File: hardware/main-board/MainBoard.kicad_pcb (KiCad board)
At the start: 4 copper layers, 145 parts, among them J1 Conn_01x03_Pin, J10 USB_C_Receptacle_USB2.0_14P, J11 Conn_02x05_Odd_Even, J12 Conn_01x02_Pin, J13 Conn_01x02_Pin, J2 Conn_01x03_Pin, J3 Conn_01x03_Pin, J4 Conn_01x03_Pin, J5 Conn_01x02_Pin, J6 Conn_01x02_Pin, J7 Conn_01x02_Pin, J8 Conn_01x02_Pin, J9 Barrel_Jack, SW1 SW_SP3T, SW2 SW_SP3T, SW3 SW_SPST, SW4 SW_SPST, U1 CD22M3494MQZ, U10 TL071, U11 CD22M3494MQZ, U12 CD22M3494MQZ, U13 TL071, U14 AD5263BRUZ200, U15 AD5263BRUZ200, U16 TL071, U17 CD22M3494MQZ, U18 CD22M3494MQZ, U19 TL071, U2 TL081, U20 AD5263BRUZ200, U21 AD5263BRUZ200, U22 TL071, U23 CD22M3494MQZ, U24 CD22M3494MQZ, U25 TL071, U26 AD5263BRUZ200, U27 AD5263BRUZ200, U28 TL071, U29 CD22M3494MQZ, U3 TL071, U30 CD22M3494MQZ, U31 XTPS55285VALR, U32 TPS54202DDC, U33 LM2776, U34 74HC164, U35 FT232RL, U36 74HC164, U37 STM32F091RCTx, U38 74HC164, U4 TL071, U5 TL071, U6 TL071, U7 TL071, U8 AD5263BRUZ200, U9 AD5263BRUZ200

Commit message: Standard cell 1 finalizations
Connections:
- net /STD/Y1 renamed /STD_Y1
- U1 pad 29: /STD/Y2 -> /STD_Y0
- U1 pad 31: /STD/Y0 -> /STD_Y2
- U11 pad 32: /STD/Y0 -> /STD_Y0
- U11 pad 37: /STD/Y2 -> /STD_Y2
- U12 pad 13: /STD/Y2 -> /STD_Y2
- U12 pad 17: /STD/Y0 -> /STD_Y0
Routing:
- net /STD_Y0: track 0.00 -> 110.1 mm, vias 0 -> 2
- net /STD_Y2: track 0.00 -> 105.1 mm, vias 0 -> 2
- net /MicroController/MT_CS_6: track 14.5 -> 109.1 mm, vias 0 -> 4
- net /MicroController/BRUZ_NCS_2: track 0.00 -> 88.0 mm, vias 0 -> 4
- net /STD_Y1: track 47.8 -> 107.6 mm
- net /MicroController/MT_CS_3: track 71.4 -> 128.7 mm, vias 2 -> 4
- net /STD/Y0: track 52.1 -> 0.00 mm, vias 2 -> 0
- net /STD/Y2: track 44.1 -> 0.00 mm, vias 2 -> 0
- net /MicroController/MT_DAT: track 229.8 -> 272.4 mm, vias 16 -> 17
- net /MicroController/BRUZ_NCS_0: track 33.6 -> 64.1 mm, vias 0 -> 2
- net /MicroController/MT_CS_8: track 46.7 -> 19.5 mm
- net /MicroController/MT_CS_7: track 70.4 -> 50.7 mm
- net /Cell_0_Buff: track 4.95 -> 7.70 mm

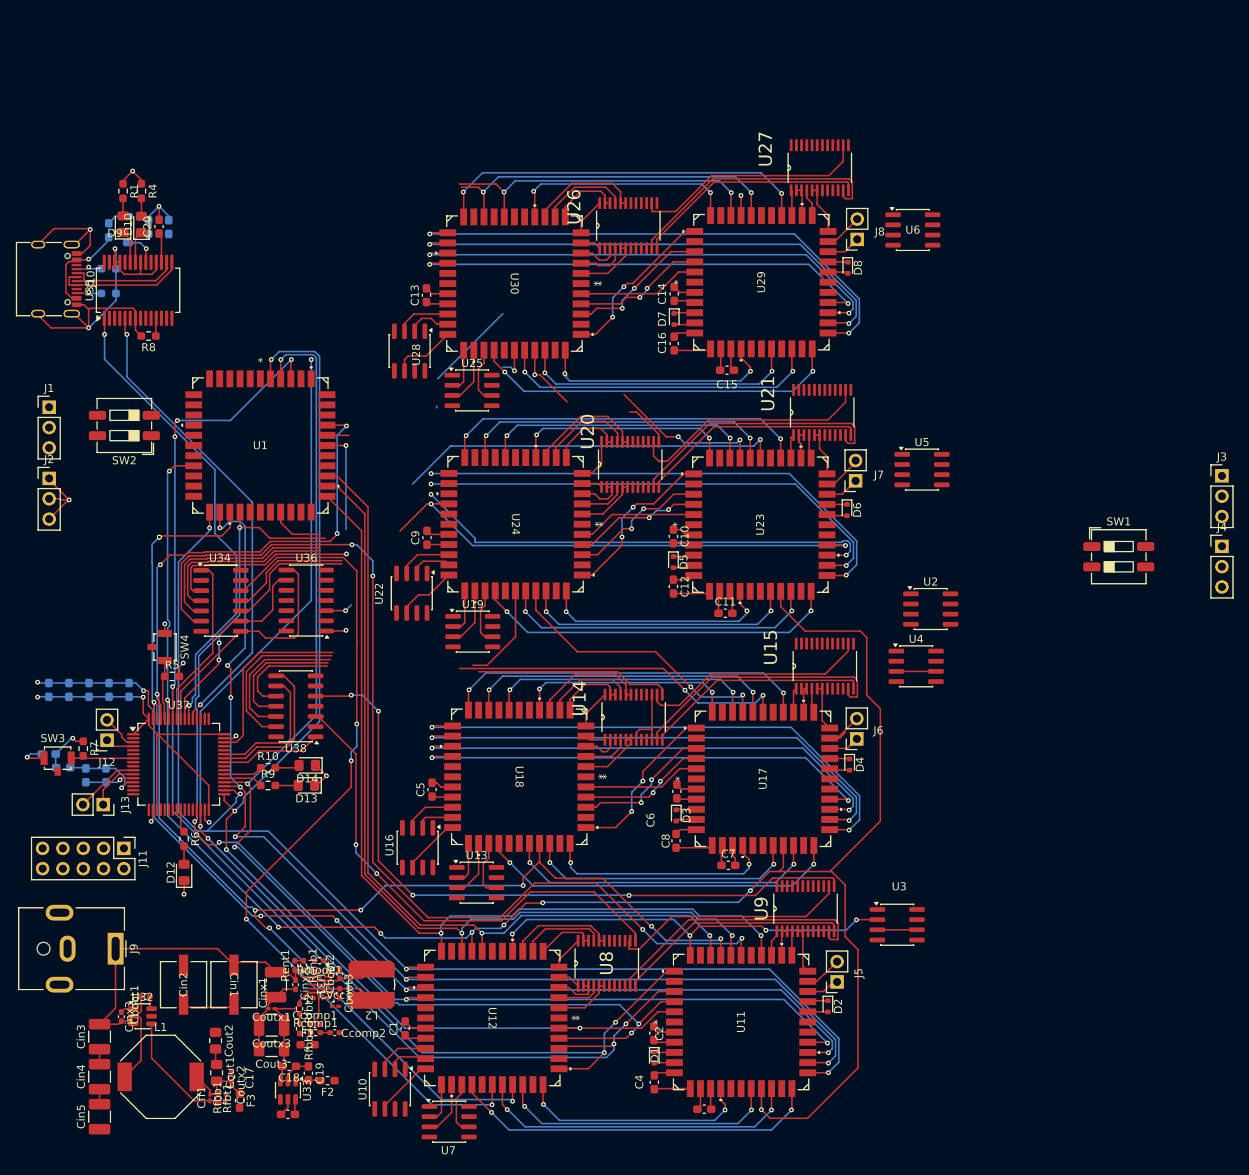
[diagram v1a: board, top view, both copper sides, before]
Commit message: linked outside AX and AY and other controls
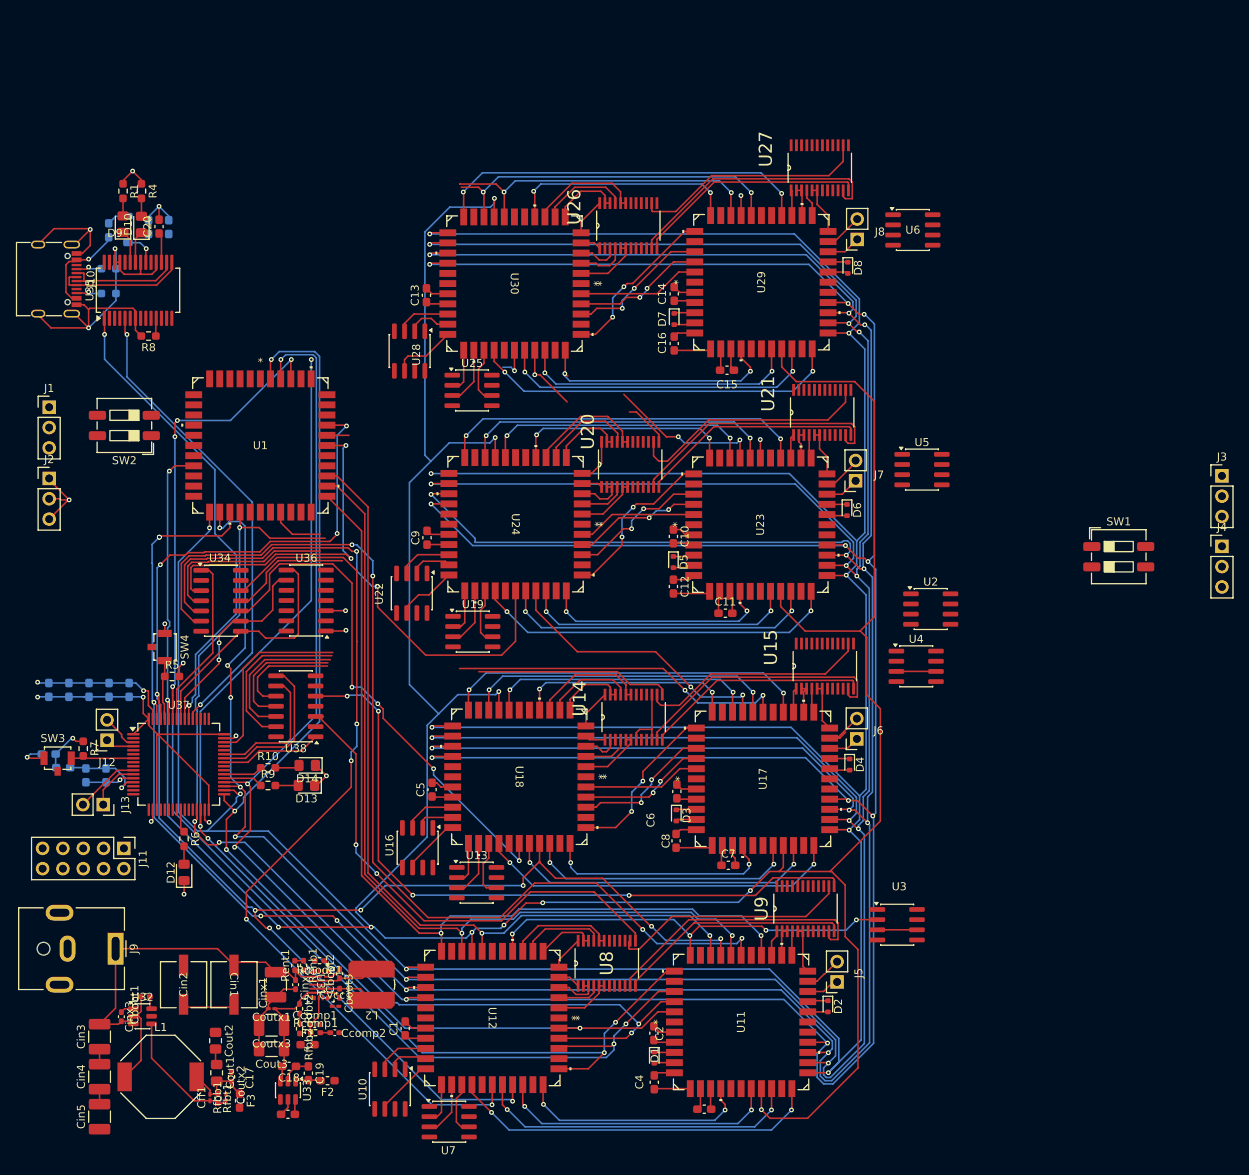
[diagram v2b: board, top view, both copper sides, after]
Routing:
- net /MicroController/MT_STB: track 238.4 -> 414.3 mm, vias 9 -> 12
- net /MicroController/MT_AY0: track 335.7 -> 449.5 mm, vias 13 -> 16
- net /MicroController/MT_AY1: track 333.0 -> 444.7 mm, vias 11 -> 14
- net /MicroController/MT_AX2: track 333.5 -> 441.1 mm, vias 13 -> 16
- net /MicroController/MT_AX1: track 349.7 -> 438.5 mm
- net /MicroController/MT_CS_4: track 16.3 -> 64.7 mm, vias 0 -> 4
- net /MicroController/MT_CS_7: track 50.7 -> 4.92 mm
- net /MicroController/MT_CS_2: track 37.6 -> 65.0 mm, vias 0 -> 2
- net /MicroController/MT_CS_8: track 19.5 -> 6.73 mm
- net /MicroController/MT_CS_0: track 37.0 -> 42.0 mm

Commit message: STD2 Analog
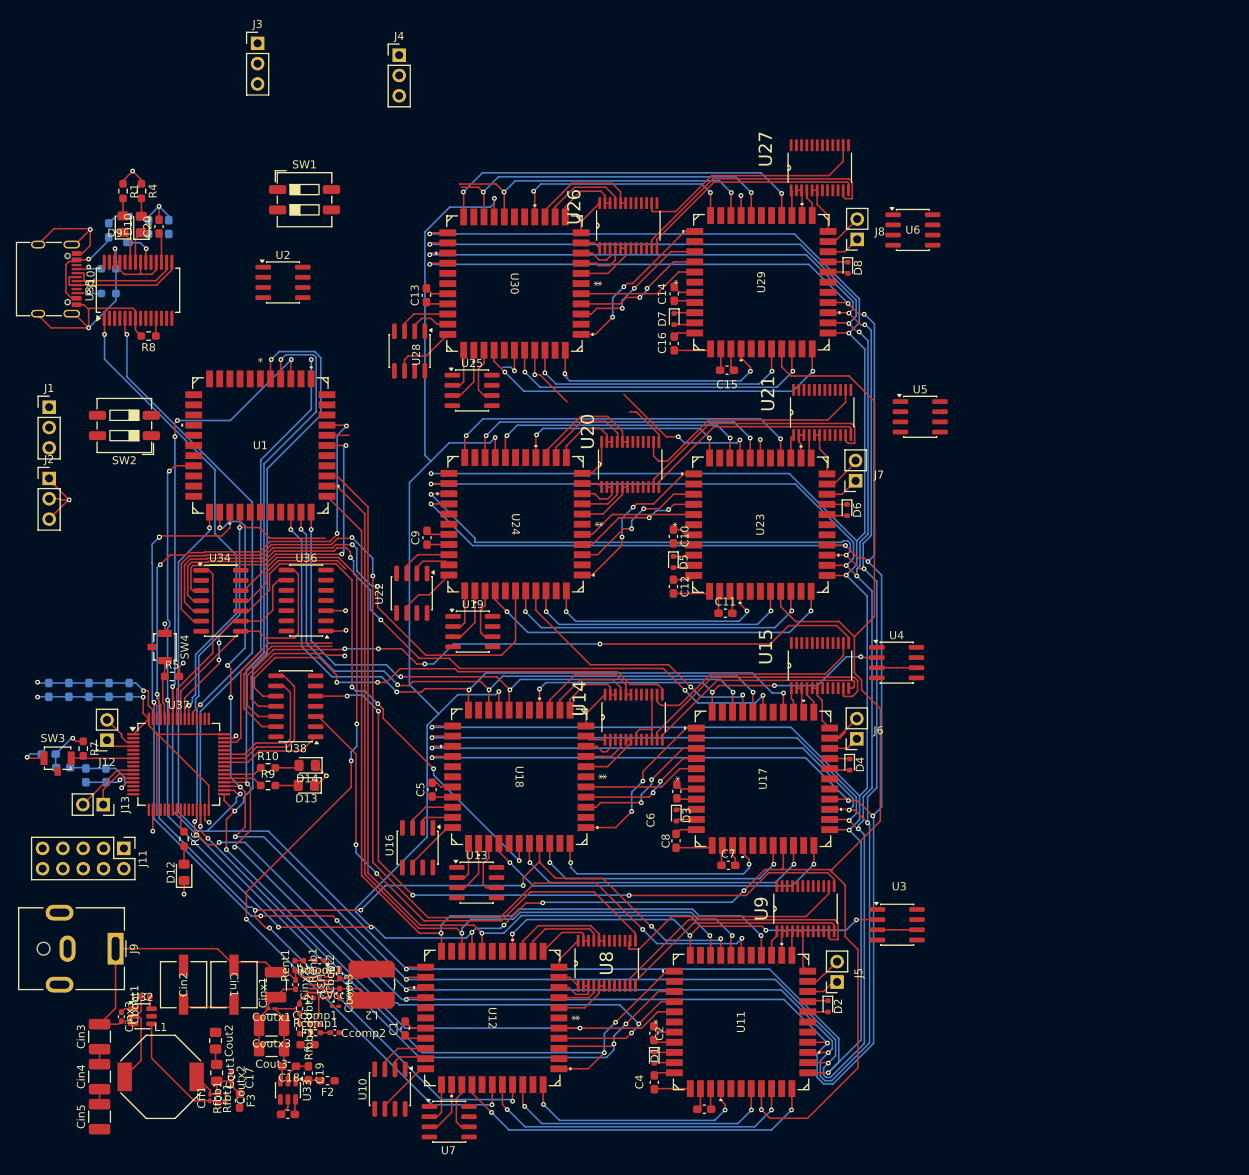
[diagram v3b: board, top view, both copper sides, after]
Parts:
- moved J3 132.1 mm to (89.3, 25.4)
- moved J4 119.8 mm to (107.0, 26.9)
- moved SW1 111.1 mm to (95.2, 45.0)
- moved U2 90.7 mm to (92.5, 55.3)
- moved U5 6.60 mm to (172.1, 72.1)
- moved U4 2.49 mm to (169.2, 102.8)
- moved U15 0.61 mm to (159.6, 103.2)
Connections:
- U1 pad 26: /STD1/Y2 -> /STD_Y0
- U1 pad 27: /STD1/Y1 -> /STD_Y1
- U1 pad 28: /STD1/Y0 -> /STD_Y2
- U17 pad 32: /STD1/Y0 -> /STD_Y0
- U17 pad 35: /STD1/Y1 -> /STD_Y1
- U17 pad 37: /STD1/Y2 -> /STD_Y2
- U18 pad 13: /STD1/Y2 -> /STD_Y2
- U18 pad 15: /STD1/Y1 -> /STD_Y1
- U18 pad 17: /STD1/Y0 -> /STD_Y0
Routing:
- net /STD_Y0: track 110.1 -> 197.3 mm, vias 2 -> 6
- net /STD_Y1: track 107.6 -> 189.6 mm, vias 2 -> 6
- net /STD_Y2: track 105.1 -> 182.7 mm, vias 2 -> 6
- net /MicroController/BRUZ_NCS_6: track 18.8 -> 88.8 mm, vias 0 -> 4
- net /STD1/Y0: track 46.2 -> 0.00 mm, vias 2 -> 0
- net /STD1/Y1: track 39.6 -> 0.00 mm, vias 2 -> 0
- net /STD1/Y2: track 34.2 -> 0.00 mm, vias 2 -> 0
- net /MicroController/MT_CS_1: track 65.2 -> 91.7 mm, vias 2 -> 4
- net /Cell_1_Out: track 27.6 -> 50.6 mm, vias 2 -> 4
- net /MicroController/BRUZ_NCS_4: track 38.2 -> 60.6 mm, vias 0 -> 2
- net /STD2/Y2: track 41.4 -> 34.5 mm
- net /MicroController/BRUZ_NCS_5: track 16.2 -> 19.3 mm, vias 0 -> 1
- net /MicroController/MT_CS_0: track 42.0 -> 39.7 mm
- net GND: track 117.1 -> 118.3 mm
- net /MicroController/MT_CS_3: track 128.7 -> 129.7 mm
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
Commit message: ran more control lines on cell 0 and 1
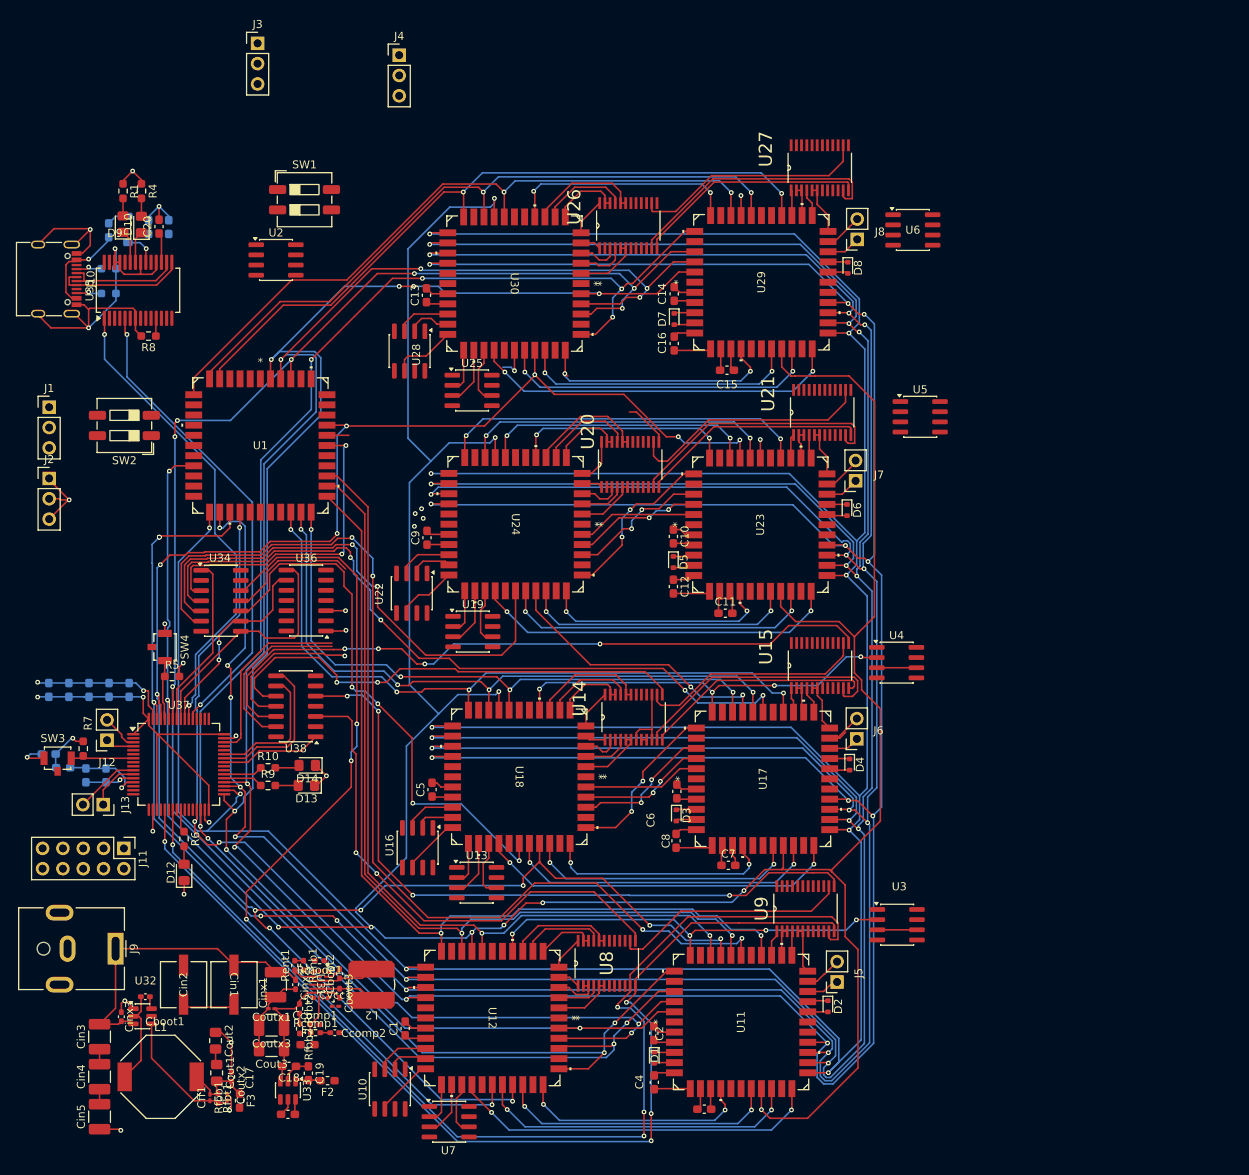
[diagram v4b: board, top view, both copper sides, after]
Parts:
- moved U2 2.94 mm to (91.6, 52.5)
- moved Rfbb1 0.16 mm to (85.5, 157.2)
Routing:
- net /MicroController/SPI1_SCK: track 115.6 -> 218.1 mm, vias 0 -> 4
- net /MicroController/SPI1_MOSI: track 134.4 -> 235.6 mm, vias 0 -> 4
- net /MicroController/MT_AX3: track 201.1 -> 252.5 mm, vias 11 -> 13
- net /MicroController/MT_RST: track 213.4 -> 261.6 mm, vias 12 -> 14
- net /STD3/Y2: track 41.6 -> 86.9 mm
- net /MicroController/MT_AX0: track 192.3 -> 237.4 mm, vias 4 -> 8
- net /MicroController/MT_AY2: track 212.8 -> 256.4 mm, vias 11 -> 13
- net /STD3/Y1: track 44.1 -> 86.0 mm
- net /STD3/Y0: track 47.8 -> 88.6 mm
- net /MicroController/MT_DAT: track 272.4 -> 305.2 mm
- net GNDPWR: track 15.8 -> 28.6 mm, vias 0 -> 4
- net /MicroController/MT_AY1: track 445.3 -> 434.4 mm
- net /MicroController/MT_CS_4: track 64.9 -> 68.5 mm
- net /MicroController/MT_STB: track 414.3 -> 416.0 mm
- net /MicroController/BRUZ_NCS_0: track 64.1 -> 65.3 mm
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
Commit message: Standard cell 2
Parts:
- moved U5 2.93 mm to (169.2, 71.7)
- moved U21 0.48 mm to (159.4, 71.5)
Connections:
- U1 pad 2: unconnected-(U1A-X14-Pad2) -> /STD2_Y0
- U1 pad 25: /STD2/Y2 -> unconnected-(U1A-X12-Pad25)
- U1 pad 26: /STD_Y0 -> /STD1_Y0
- U1 pad 27: /STD_Y1 -> /STD1_Y1
- U1 pad 28: /STD_Y2 -> /STD1_Y2
- U1 pad 3: unconnected-(U1A-X15-Pad3) -> /STD2_Y1
- U1 pad 4: Net-(U1A-X6) -> /STD2_Y2
- U1 pad 8: /STD2/Y0 -> /STD_Out
- U1 pad 9: /STD2/Y1 -> unconnected-(U1A-X11-Pad9)
- U17 pad 32: /STD_Y0 -> /STD1_Y0
- U17 pad 35: /STD_Y1 -> /STD1_Y1
- U17 pad 37: /STD_Y2 -> /STD1_Y2
- U18 pad 13: /STD_Y2 -> /STD1_Y2
- U18 pad 15: /STD_Y1 -> /STD1_Y1
- U18 pad 17: /STD_Y0 -> /STD1_Y0
- U2 pad 3: Net-(U1A-X6) -> /STD_Out
- U23 pad 32: /STD2/Y0 -> /STD2_Y0
- U23 pad 35: /STD2/Y1 -> /STD2_Y1
- U23 pad 37: /STD2/Y2 -> /STD2_Y2
- U24 pad 13: /STD2/Y2 -> /STD2_Y2
- U24 pad 15: /STD2/Y1 -> /STD2_Y1
- U24 pad 17: /STD2/Y0 -> /STD2_Y0
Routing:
- net /MicroController/BRUZ_NCS_3: track 0.00 -> 99.4 mm, vias 0 -> 4
- net /MicroController/MT_CS_7: track 4.92 -> 95.4 mm, vias 2 -> 5
- net /STD1_Y0: track 0.00 -> 87.2 mm, vias 0 -> 2
- net /STD_Y0: track 197.2 -> 110.1 mm, vias 6 -> 4
- net /STD2_Y0: track 0.00 -> 84.1 mm, vias 0 -> 4
- net /STD1_Y1: track 0.00 -> 82.0 mm, vias 0 -> 2
- net /STD_Y1: track 189.6 -> 107.6 mm, vias 6 -> 4
- net /STD2_Y1: track 0.00 -> 81.6 mm, vias 0 -> 4
- net /STD2_Y2: track 0.00 -> 80.8 mm, vias 0 -> 4
- net /STD1_Y2: track 0.00 -> 77.7 mm, vias 0 -> 2
- net /STD_Y2: track 182.7 -> 105.1 mm, vias 6 -> 4
- net /MicroController/BRUZ_NCS_1: track 5.77 -> 74.9 mm, vias 0 -> 2
- net /MicroController/MT_DAT: track 305.2 -> 360.7 mm, vias 17 -> 18
- net /MicroController/MT_CS_8: track 6.73 -> 53.9 mm, vias 2 -> 3
- net /STD2/Y0: track 46.5 -> 0.00 mm, vias 2 -> 0
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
